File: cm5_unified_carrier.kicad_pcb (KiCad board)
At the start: 4 copper layers, 139 x 77 mm, 41 parts, among them J101 436500403, J102 484050003, J103 484050003, J201 7499511002A, J401 PJ-102AH, U201 AG5712-LPB, U501 Hirose DF40C-100DS-0.4V

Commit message: Added another barrel jack for 12V output for ASI camera
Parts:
- removed U501: Hirose DF40C-100DS-0.4V, footprints:Radxa_CM5
- added C103: 10uF, Capacitor_SMD:C_1206_3216Metric_Pad1.33x1.80mm_HandSolder, F.Cu at (101.0, 75.8)
- added J104: PJ-102AH, PJ-102AH:CUI_PJ-102AH, F.Cu at (96.9, 66.8)
- added J501: Hirose DF40C-100DS-0.4V, CM5 module:Radxa_CM5, F.Cu at (197.0, 65.2)
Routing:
- net /V12_BUS: track 22.8 -> 34.1 mm, vias 12 -> 19
- net GND: track 166.6 -> 175.9 mm, vias 63 -> 69
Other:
- board text added: "12V for ASI cooler"

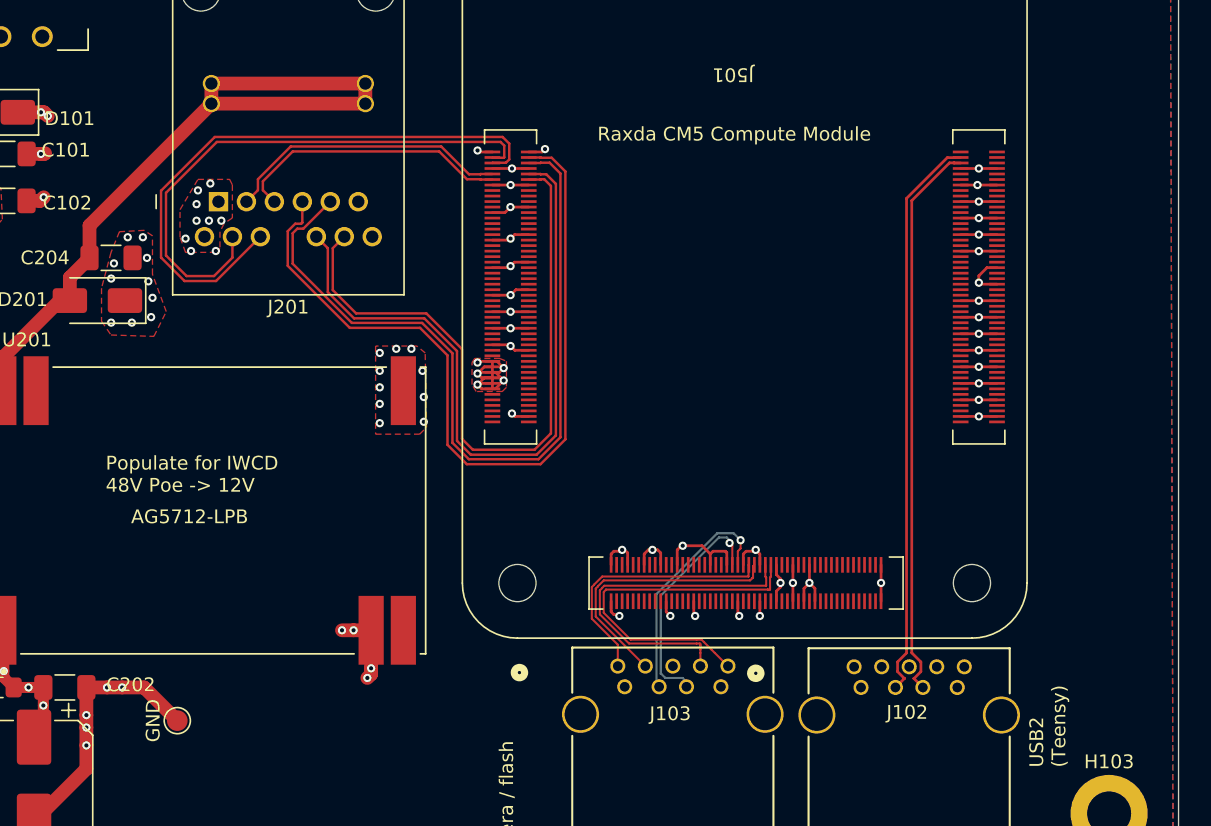
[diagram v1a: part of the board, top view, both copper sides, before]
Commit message: Added USB connector for flashing eMMC and related switches
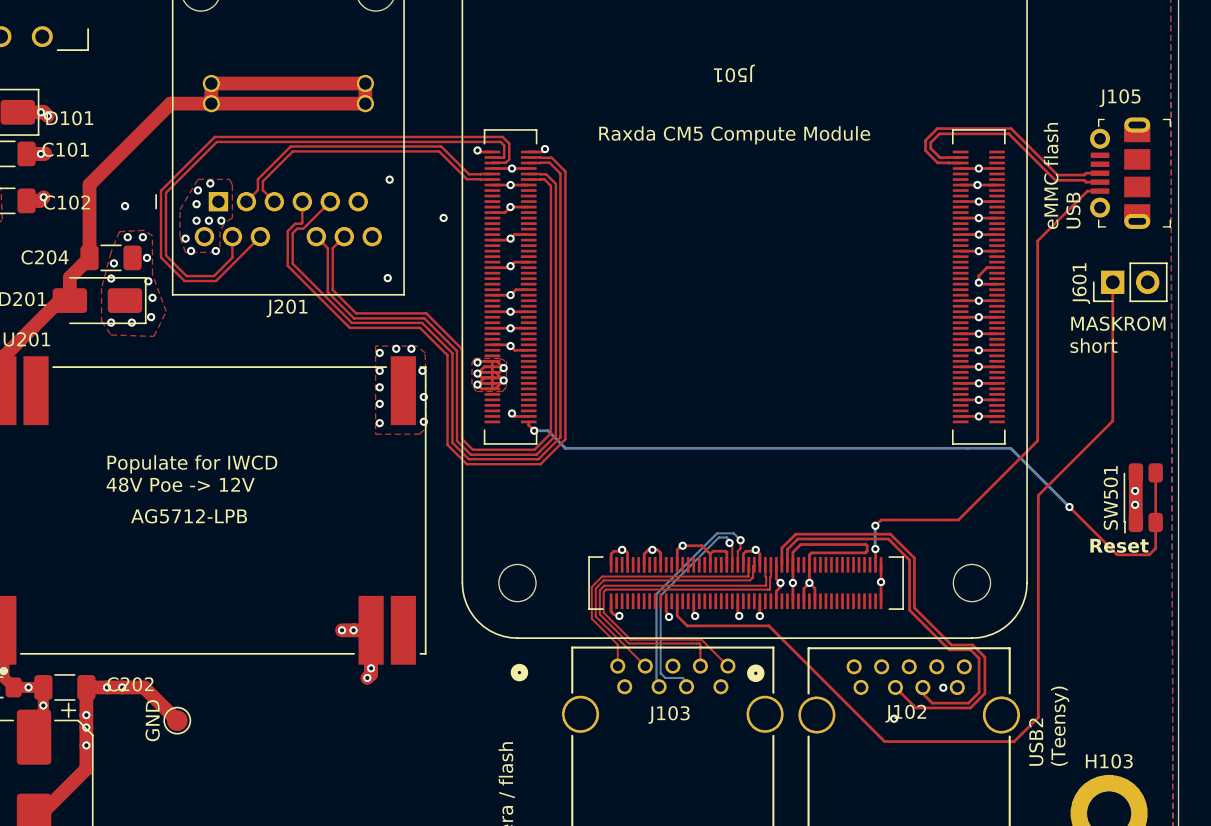
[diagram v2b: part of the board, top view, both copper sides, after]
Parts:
- added J105: 1050170001, digikey-footprints:USB_Micro_B_Female_1050170001, F.Cu at (206.3, 83.5)
- added J601: Conn_01x02_Pin, Connector_PinHeader_2.54mm:PinHeader_1x02_P2.54mm_Vertical, F.Cu at (207.2, 91.4)
- added SW501: SW_Push, Button_Switch_SMD:SW_SPST_EVQP7A, F.Cu at (209.6, 107.0)
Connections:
- J102 pad 2: /CM5_Core/USB2_N -> /CM5_HighSpeed/USB2_HOST2_DP
- J102 pad 3: /CM5_Core/USB2_P -> /CM5_HighSpeed/USB2_HOST2_DM
- J501 pad 100: unconnected-(J501A-nEXTRST-Pad100) -> Net-(J501A-nEXTRST)
- J501 pad 226: unconnected-(J501C-SARADC_VIN0_KEY/RECOVERY-Pad226) -> /CM5_HighSpeed/KEY/RECOVERY
- J501 pad 263: unconnected-(J501C-USB2_HOST2_DP-Pad263) -> /CM5_HighSpeed/USB2_HOST2_DP
- J501 pad 265: unconnected-(J501C-USB2_HOST2_DM-Pad265) -> /CM5_HighSpeed/USB2_HOST2_DM
- J501 pad 297: unconnected-(J501C-USB_OTG0_VBUSDET-Pad297) -> /CM5_HighSpeed/USB_OTG0_VBUSDET
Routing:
- net /CM5_HighSpeed/KEY/RECOVERY: track 0.00 -> 65.6 mm
- net Net-(J501A-nEXTRST): track 0.00 -> 55.4 mm, vias 0 -> 2
- net /CM5_HighSpeed/USB_OTG0_VBUSDET: track 0.00 -> 37.9 mm, vias 0 -> 2
- net /CM5_HighSpeed/USB2_HOST2_DP: track 0.00 -> 32.4 mm
- net /CM5_HighSpeed/USB2_HOST2_DM: track 0.00 -> 29.0 mm
- net /CM5_Core/USB2_N: track 41.4 -> 16.9 mm
- net /CM5_Core/USB2_P: track 40.8 -> 18.1 mm
- net GND: track 175.9 -> 191.5 mm, vias 69 -> 77
- net Net-(D201-A2): track 52.8 -> 54.5 mm
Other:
- board text added: "MASKROM short"
- board text added: "Reset"
- board text added: "eMMC flash USB"

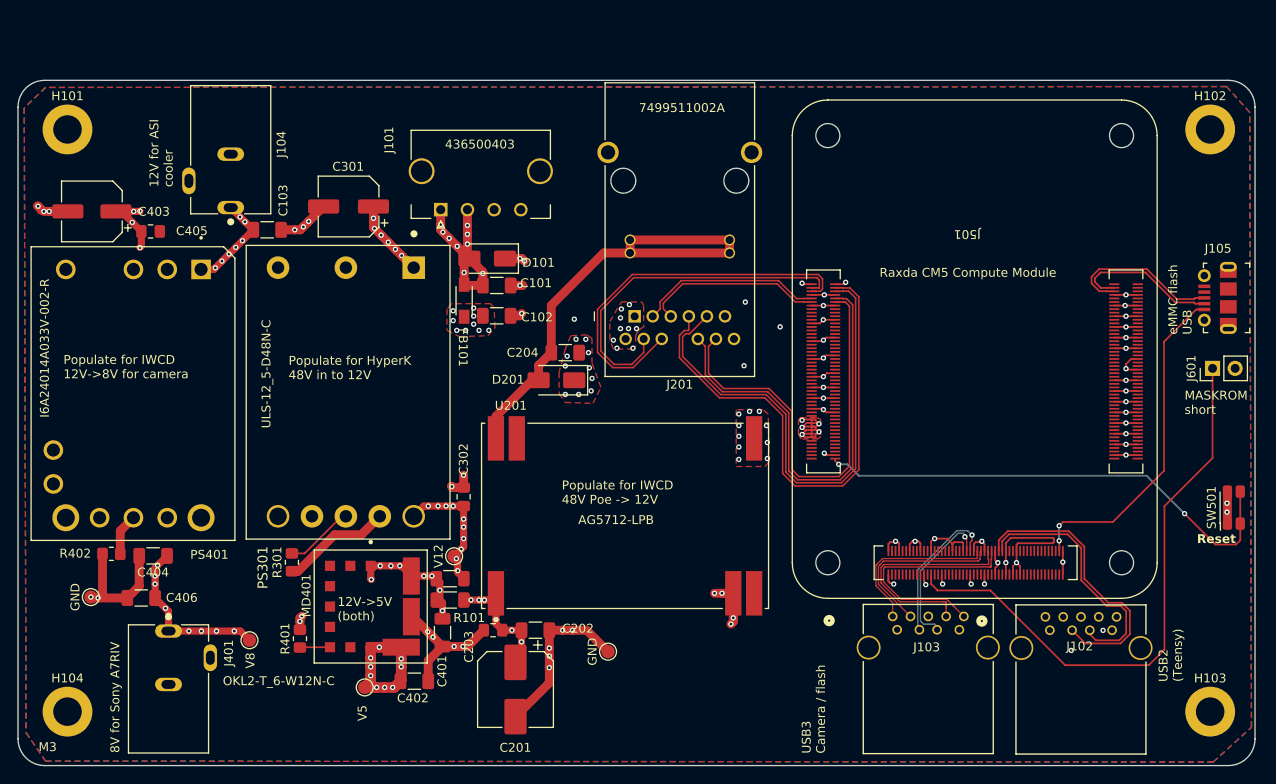
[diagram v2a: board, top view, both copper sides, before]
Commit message: Reduced board size by allowing overlap of power modules where only one needs to be populated
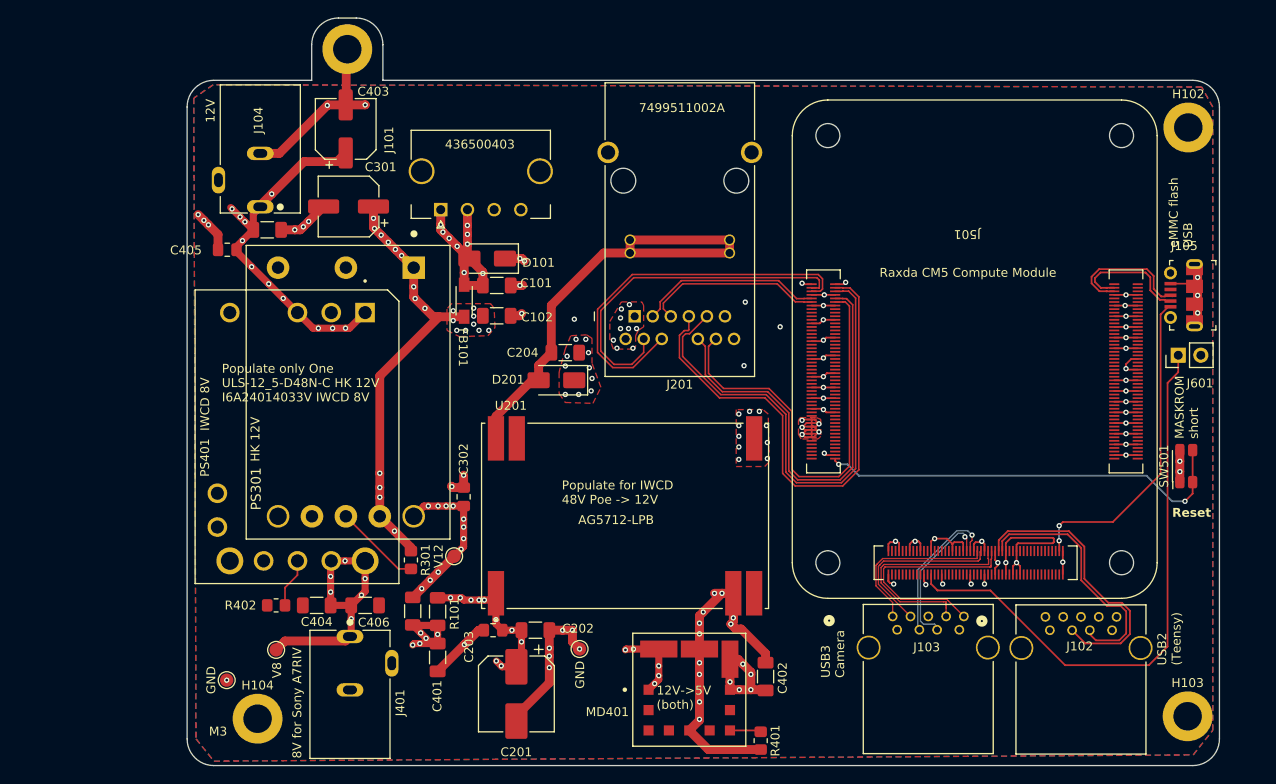
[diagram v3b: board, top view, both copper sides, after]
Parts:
- removed TP402: V5, TestPoint:TestPoint_Pad_D1.5mm
- moved R401 53.0 mm to (156.4, 133.2), turned to -90 degrees
- moved C402 39.5 mm to (157.0, 126.0), turned to 90 degrees
- moved MD401 37.0 mm to (148.4, 127.5), turned to 0 degrees
- moved H101 32.7 mm to (110.0, 55.5)
- moved C403 30.0 mm to (109.8, 64.5), turned to 90 degrees
- moved C406 25.2 mm to (112.0, 118.0), turned to 0 degrees
- moved H104 21.4 mm to (99.9, 130.7)
- moved J401 20.4 mm to (110.3, 128.0)
- moved R402 19.4 mm to (102.0, 118.0)
- moved C404 19.2 mm to (106.6, 118.0)
- moved PS401 19.1 mm to (104.3, 99.0)
- moved TP403 17.9 mm to (96.5, 126.4)
- moved R301 13.4 mm to (117.2, 112.9), turned to -90 degrees
- moved C405 8.86 mm to (96.5, 78.0), turned to 180 degrees
- moved SW501 7.09 mm to (204.3, 102.3)
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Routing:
- net GND: track 191.5 -> 227.2 mm, vias 77 -> 82
- net /VIN_MURATA: track 21.2 -> 49.2 mm, vias 15 -> 22
- net /V12_BUS: track 34.1 -> 60.2 mm, vias 19 -> 21
- net /Power_12_to_5_8/V8_FROM_12: track 19.1 -> 29.3 mm, vias 9 -> 6
- net Net-(J501A-nEXTRST): track 55.4 -> 47.5 mm
- net /Ethernet_PoE/V12_FROM_POE: track 14.4 -> 20.0 mm, vias 6 -> 10
- net +5V: track 31.7 -> 27.7 mm, vias 14 -> 10
- net /Power_48_to_12_5/V12_FROM_48: track 15.1 -> 18.7 mm, vias 10 -> 11
- net /CM5_Core/USB2_N: track 16.9 -> 13.8 mm
- net /CM5_Core/USB2_P: track 18.1 -> 15.3 mm
- net Net-(PS301-TRIM): track 7.79 -> 9.76 mm
- net /CM5_HighSpeed/USB_OTG0_VBUSDET: track 37.9 -> 36.7 mm
- net Net-(PS401-TRIM): track 4.67 -> 5.58 mm
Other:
- board size 139 x 77 mm -> 116 x 84 mm
- board text added: "0.0000 mm / 0.0000 mm"
- board text added: "0.3000 mm"
- board text added: "1.6000 mm"
- board text added: "116.0000 mm x 84.0000 mm"
- board text added: "12V"
- board text added: "4"
- board text added: "BOARD CHARACTERISTICS"
- board text added: "Board Thickness:"
- board text added: "Board overall dimensions:"
- board text added: "Castellated pads:"
- board text added: "Copper Finish:"
- board text added: "Copper Layer Count:"
- board text added: "Edge card connectors:"
- board text added: "HK 12V"
- board text added: "IWCD 8V"
- board text added: "Impedance Control:"
- board text added: "Min hole diameter:"
- board text added: "Min track/spacing:"
- board text added: "No"
- board text added: "None"
- board text added: "Plated Board Edge:"
- board text added: "Populate only One ULS-12_5-D48N-C HK 12V I6A24014033V IWCD 8V"
- board text added: "USB3 Camera"
- board text removed: "12V for ASI cooler"
- board text removed: "Populate for HyperK 48V in to 12V"
- board text removed: "Populate for IWCD 12V->8V for camera"
- board text removed: "USB3 Camera / flash"
